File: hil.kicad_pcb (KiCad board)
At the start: 2 copper layers, 188 x 55.9 mm, 65 parts, among them J1 5V In, J10 +3V3, J11 GND, J12 Programming Connector, J13 PPS IO, J14 Power Input, J15 PPS IO, J16 Power Input, J17 PPS IO, J18 Power Input, J19 PPS IO, J2 USB_B, J20 Power Input, J21 PPS IO, J22 Power Input, J23 PPS IO, J24 Power Input, J25 PPS IO, J26 Power Input, J27 PPS IO, J28 Power Input, J29 PPS IO, J3 IO A, J30 Power Input, J31 PPS IO, J32 Power Input, J4 IO B, J7 CAN, J8 I2C, J9 +5V, U1 MCP2515, U2 AZ1117-3.3, U3 MCP2562, U4 PIC24FJ128GC010, Y1 16 MHz, Y2 48 MHz DNP

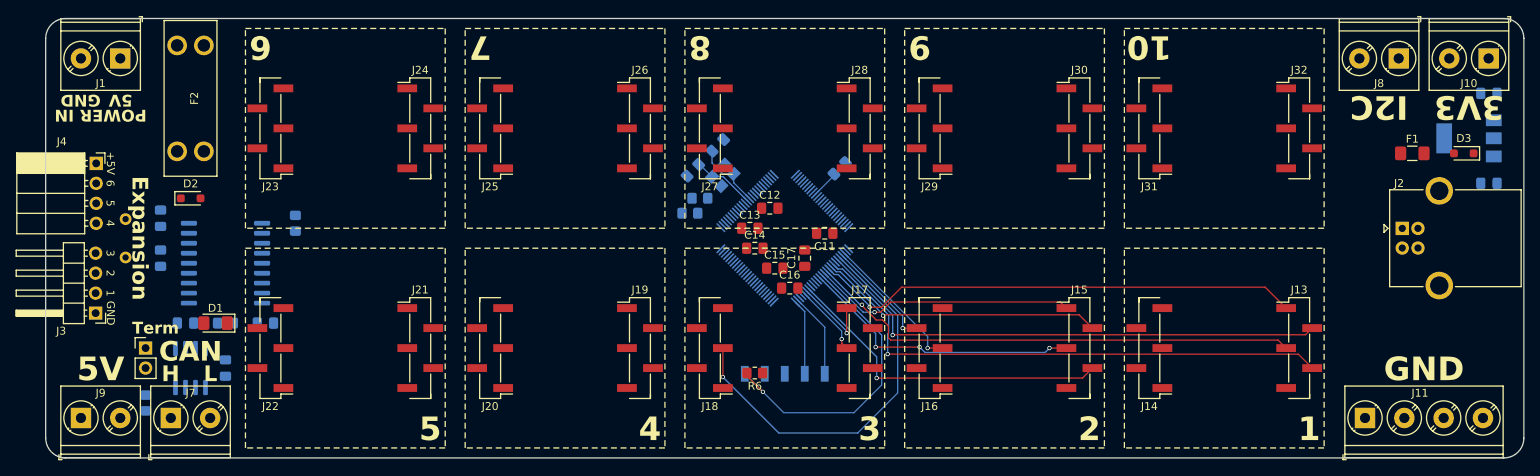
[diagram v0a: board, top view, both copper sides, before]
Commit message: Address review comments, finish routing HILT main board
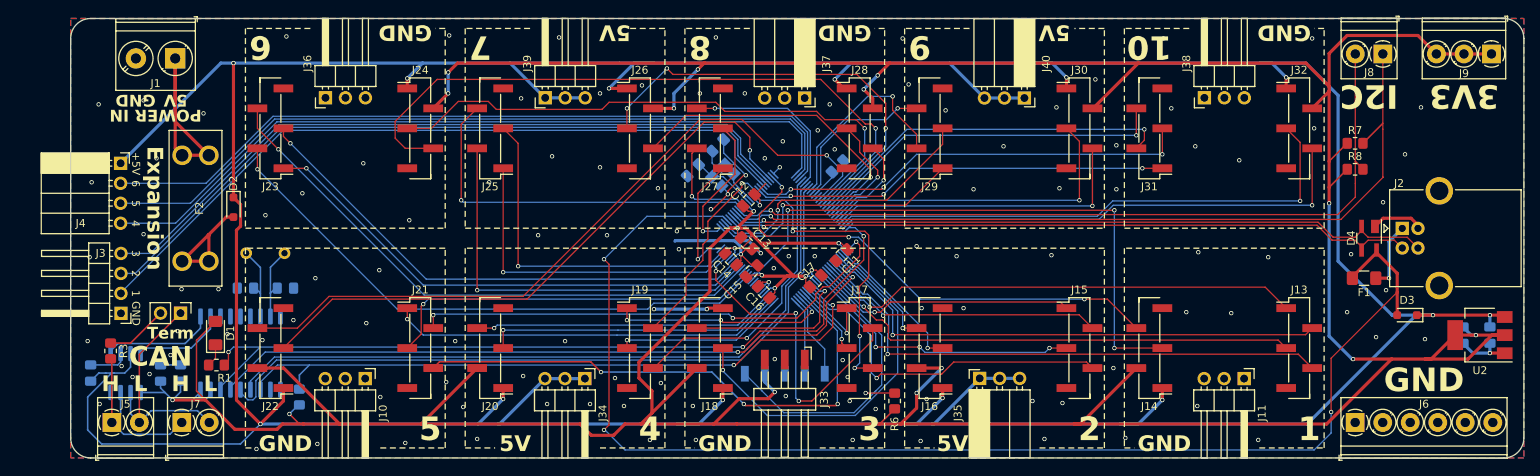
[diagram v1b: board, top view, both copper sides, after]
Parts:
- removed R4, R5: 15R, Resistor_SMD:R_0805_2012Metric_Pad1.20x1.40mm_HandSolder
- added D4: ESDALD05UJ2X, Package_TO_SOT_SMD:SOT-143_Handsoldering, F.Cu at (213.4, 127.6)
- added J33: GND2, Connector_Harwin:Harwin_M20-89003xx_1x03_P2.54mm_Horizontal, F.Cu at (139.1, 148.6)
- added J34: 5V1, Connector_PinHeader_2.54mm:PinHeader_1x03_P2.54mm_Horizontal, F.Cu at (113.7, 145.5)
- added J35: 5V2, Connector_PinSocket_2.54mm:PinSocket_1x03_P2.54mm_Horizontal, F.Cu at (163.8, 145.5)
- added J36: GND4, Connector_PinHeader_2.54mm:PinHeader_1x03_P2.54mm_Horizontal, F.Cu at (80.7, 109.8)
- added J37: GND5, Connector_PinSocket_2.54mm:PinSocket_1x03_P2.54mm_Horizontal, F.Cu at (141.6, 109.8)
- added J38: GND6, Connector_PinHeader_2.54mm:PinHeader_1x03_P2.54mm_Horizontal, F.Cu at (192.4, 109.8)
- added J39: 5V3, Connector_PinHeader_2.54mm:PinHeader_1x03_P2.54mm_Horizontal, F.Cu at (108.6, 109.8)
- added J40: 5V4, Connector_PinSocket_2.54mm:PinSocket_1x03_P2.54mm_Horizontal, F.Cu at (169.5, 109.8)
- added J5: CAN B, TerminalBlock_Phoenix:TerminalBlock_Phoenix_PT-1,5-2-3.5-H_1x02_P3.50mm_Horizontal, F.Cu at (53.5, 151.1)
- added J6: GND, TerminalBlock_Phoenix:TerminalBlock_Phoenix_PT-1,5-6-3.5-H_1x06_P3.50mm_Horizontal, F.Cu at (211.6, 151.1)
- added R7: 4.7k, Resistor_SMD:R_0805_2012Metric_Pad1.20x1.40mm_HandSolder, F.Cu at (211.6, 115.6)
- added R8: 4.7k, Resistor_SMD:R_0805_2012Metric_Pad1.20x1.40mm_HandSolder, F.Cu at (211.6, 118.9)
- C4, C5: value C -> 27p
- J10: value +3V3 -> GND1; footprint TerminalBlock_Phoenix:TerminalBlock_Phoenix_PT-1,5-2-5.0-H_1x02_P5.00mm_Horizontal -> Connector_PinHeader_2.54mm:PinHeader_1x03_P2.54mm_Horizontal
- J11: value GND -> GND3; footprint TerminalBlock_Phoenix:TerminalBlock_Phoenix_PT-1,5-4-5.0-H_1x04_P5.00mm_Horizontal -> Connector_PinHeader_2.54mm:PinHeader_1x03_P2.54mm_Horizontal
- J7: value CAN -> CAN A; footprint TerminalBlock_Phoenix:TerminalBlock_Phoenix_PT-1,5-2-5.0-H_1x02_P5.00mm_Horizontal -> TerminalBlock_Phoenix:TerminalBlock_Phoenix_PT-1,5-2-3.5-H_1x02_P3.50mm_Horizontal
- J8: footprint TerminalBlock_Phoenix:TerminalBlock_Phoenix_PT-1,5-2-5.0-H_1x02_P5.00mm_Horizontal -> TerminalBlock_Phoenix:TerminalBlock_Phoenix_PT-1,5-2-3.5-H_1x02_P3.50mm_Horizontal
- J9: value +5V -> 3V3; footprint TerminalBlock_Phoenix:TerminalBlock_Phoenix_PT-1,5-2-5.0-H_1x02_P5.00mm_Horizontal -> TerminalBlock_Phoenix:TerminalBlock_Phoenix_PT-1,5-3-3.5-H_1x03_P3.50mm_Horizontal
- R1: value 260R -> 270R; moved to F.Cu
- R3, U2: moved to F.Cu
- Y1: value 16 MHz -> 12 MHz
- moved J9 185.2 mm to (228.9, 104.2), turned to 180 degrees
- moved J10 148.5 mm to (85.7, 145.5), turned to -90 degrees
- moved C7 30.9 mm to (225.3, 140.0), turned to -90 degrees
- moved U2 25.1 mm to (227.5, 140.0)
- moved R2 22.1 mm to (77.3, 147.8), turned to 90 degrees
- moved D3 21.8 mm to (218.2, 137.4)
- moved C2 19.3 mm to (228.7, 140.0), turned to -90 degrees
- moved C4 18.2 mm to (75.6, 134.0), turned to 0 degrees
- moved R6 18.1 mm to (153.0, 148.3), turned to 90 degrees
- moved F1 17.0 mm to (212.7, 132.7), turned to 180 degrees
- moved J11 16.2 mm to (197.5, 145.5), turned to -90 degrees
- moved Y1 15.3 mm to (70.6, 129.5), turned to 0 degrees
- moved F2 14.0 mm to (64.1, 123.8)
- moved C6 13.6 mm to (50.8, 144.8), turned to 90 degrees
- moved C1 12.5 mm to (62.2, 144.8), turned to 90 degrees
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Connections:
- J10 pad 1: +3V3 -> GND
- J10 pad 2: +3V3 -> GND
- J9 pad 1: +5V -> +3V3
- J9 pad 2: +5V -> +3V3
- U4 pad 56: Net-(U4-D-/RG3) -> /D-
- U4 pad 57: Net-(U4-D+/RG2) -> /D+
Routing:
- net +3V3: track 0.00 -> 604.2 mm, vias 0 -> 21
- net +5V: track 0.00 -> 572.0 mm, vias 0 -> 13
- net /VUSB: track 0.00 -> 170.5 mm, vias 0 -> 3
- net /SCL: track 0.00 -> 104.5 mm, vias 0 -> 1
- net /~{CS}: track 0.00 -> 102.2 mm, vias 0 -> 3
- net /SDA: track 0.00 -> 99.8 mm, vias 0 -> 1
- net /IO5: track 0.00 -> 98.0 mm
- net /IO6: track 0.00 -> 98.0 mm
- net /IO4: track 0.00 -> 98.0 mm
- net /IO1: track 0.00 -> 94.4 mm
- net /IO2: track 0.00 -> 93.8 mm
- net /MOSI: track 0.00 -> 93.2 mm
- net /IO3: track 0.00 -> 93.1 mm
- net /D14: track 0.00 -> 92.8 mm, vias 0 -> 1
- net /D+: track 0.00 -> 90.7 mm, vias 0 -> 1
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- added copper zone on B.Cu, net GND
- added copper zone on F.Cu, net GND
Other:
- board size 188 x 55.9 mm -> 184.8 x 55.9 mm

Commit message: Address review comments
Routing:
- net Net-(J1-Pin_1): track 30.2 -> 26.8 mm
- net Net-(D2-A): track 15.6 -> 12.2 mm
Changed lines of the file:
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@@
   (gr_line (start 199.39 154.305) (end 207.645 154.305)
     (stroke (width 0.15) (type dash)) (layer "F.SilkS"))
+  (gr_circle (center 90.17 150.495) (end 94.92 150.495)
+    (stroke (width 0.15) (type default)) (fill none) (layer "Dwgs.User"))
   (gr_line (start 216.535 127.635) (end 216.535 127.635)
     (stroke (width 0.15) (type dot)) (layer "Dwgs.User"))
+  (gr_circle (center 90.17 104.775) (end 94.92 104.775)
+    (stroke (width 0.15) (type default)) (fill none) (layer "Dwgs.User"))
+  (gr_circle (center 204.47 150.495) (end 209.22 150.495)
+    (stroke (width 0.15) (type default)) (fill none) (layer "Dwgs.User"))
+  (gr_circle (center 204.47 104.775) (end 209.22 104.775)
+    (stroke (width 0.15) (type default)) (fill none) (layer "Dwgs.User"))
   (gr_line (start 38.1 127.635) (end 242.57 127.635)
     (stroke (width 0.15) (type dot)) (layer "Dwgs.User"))
@@
   (segment (start 65.835 127.303) (end 65.7635 127.2315) (width 0.4064) (layer "F.Cu") (net 10))
   (segment (start 62.435 130.56) (end 65.7635 127.2315) (width 0.4064) (layer "F.Cu") (net 10))
-  (segment (start 62.435 130.56) (end 65.835 130.56) (width 0.4064) (layer "F.Cu") (net 10))
   (segment (start 65.7635 127.2315) (end 68.047 124.948) (width 0.4064) (layer "F.Cu") (net 10))
   (segment (start 68.047 124.948) (end 68.961 124.948) (width 0.4064) (layer "F.Cu") (net 10))
@@
   (segment (start 61.555 104.775) (end 61.555 116.21) (width 0.4064) (layer "F.Cu") (net 12))
   (segment (start 61.555 116.21) (end 62.435 117.09) (width 0.4064) (layer "F.Cu") (net 12))
-  (segment (start 62.435 117.09) (end 65.835 117.09) (width 0.4064) (layer "F.Cu") (net 12))
   (segment (start 61.555 112.81) (end 65.835 117.09) (width 0.4064) (layer "F.Cu") (net 12))
   (segment (start 61.555 104.775) (end 61.555 112.81) (width 0.4064) (layer "F.Cu") (net 12))
